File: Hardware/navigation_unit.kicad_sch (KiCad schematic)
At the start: 36 parts, among them SW1 SW_SPDT, SW2 SW_Push_Dual, U4 STM32F405RGTx, Y1 25MHz

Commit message: hardware version 0.1.2, minor improvements and footprint selection (missing some gnss and bulk regulator components
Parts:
- SW1: footprint (none) -> Button_Switch_SMD:SW_SPDT_PCM12
- SW2: footprint (none) -> Aircraft_Footprints:SW_SKRPACE010
- Y1: footprint (none) -> Crystal:Crystal_SMD_Abracon_ABM8G-4Pin_3.2x2.5mm
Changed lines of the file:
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@@
 	(title_block
 		(title "Navigation Unit")
-		(rev "0.1.0")
+		(rev "0.1.2")
 		(company "Breno Soares Alves")
 	)
@@
 			)
 		)
-		(property "Footprint" ""
+		(property "Footprint" "Button_Switch_SMD:SW_SPDT_PCM12"
 			(at 186.69 105.41 0)
 			(effects
@@
 			)
 		)
-		(property "Footprint" ""
+		(property "Footprint" "Aircraft_Footprints:SW_SKRPACE010"
 			(at 238.76 88.9 0)
 			(effects
@@
 			)
 		)
-		(property "Footprint" ""
+		(property "Footprint" "Crystal:Crystal_SMD_Abracon_ABM8G-4Pin_3.2x2.5mm"
 			(at 157.48 66.04 0)
 			(effects

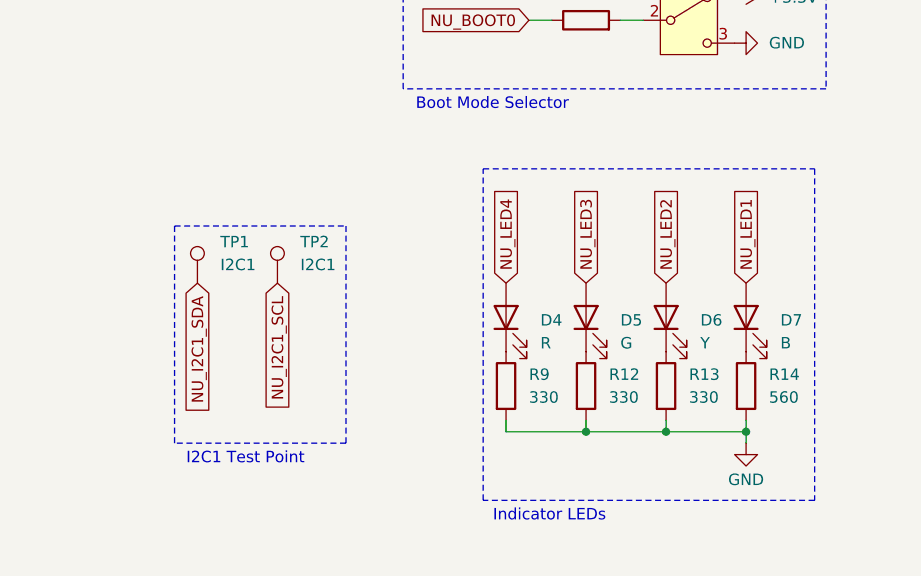
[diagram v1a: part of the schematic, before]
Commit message: board placement, no trails, just pain
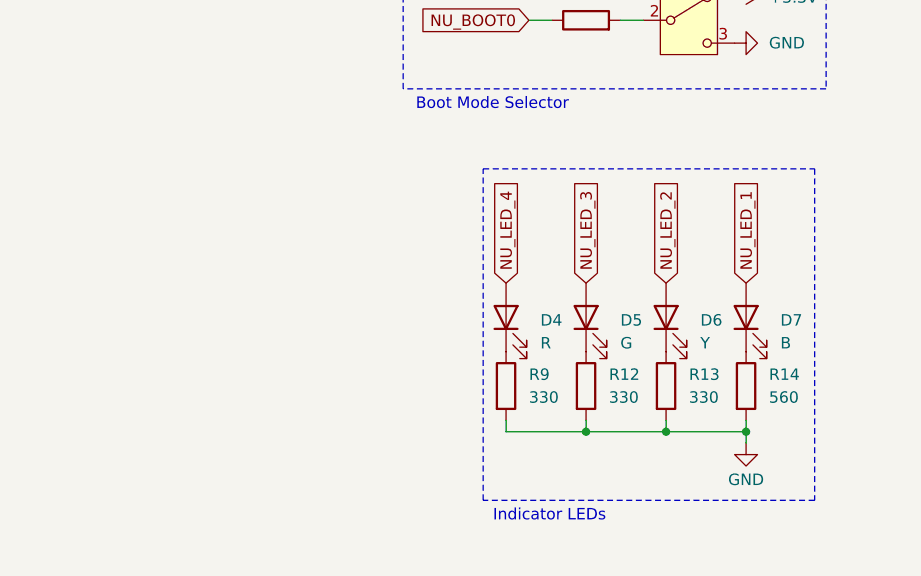
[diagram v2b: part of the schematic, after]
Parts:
- removed TP1, TP2: I2C1, TestPoint:TestPoint_Pad_D2.5mm, symbol Connector:TestPoint
- C12, C13: Digikey_Link (none) -> https://www.digikey.com.br/pt/products/detail/samsung-elect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; MPN (none) -> CL10B225KP8NNNC
- C14: footprint Capacitor_Tantalum_SMD:CP_EIA-1608-08_AVX-J -> Capacitor_SMD:C_1206_3216Metric_Pad1.33x1.80mm_HandSolder; Digikey_Link (none) -> https://www.digikey.com.br/pt/products/detail/kyocera-avx/T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; MPN (none) -> TAJA106K010TNJ
- C15, C18: Digikey_Link (none) -> https://www.digikey.com.br/pt/products/detail/w%C3%BCrth-el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; MPN (none) -> 885012005007
- C16, C17, C19, C20, C21, C22, C23, C24: Digikey_Link (none) -> https://www.digikey.com.br/pt/products/detail/samsung-elect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; MPN (none) -> CL05B104KP5NNNC
- C25: Digikey_Link (none) -> https://www.digikey.com.br/pt/products/detail/kemet/C0603C1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; MPN (none) -> C0603C104K8RACTU
- C26: Digikey_Link (none) -> https://www.digikey.com.br/pt/products/detail/kemet/T491A10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; MPN (none) -> T491A105K010AT
- D4: footprint LED_SMD:LED_0805_2012Metric -> LED_SMD:LED_0805_2012Metric_Pad1.15x1.40mm_HandSolder; Digikey_Link (none) -> https://www.digikey.com.br/pt/products/detail/liteon/LTST-C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; MPN (none) -> LTST-C171KRKT
- D5: footprint LED_SMD:LED_0805_2012Metric -> LED_SMD:LED_0805_2012Metric_Pad1.15x1.40mm_HandSolder; Digikey_Link (none) -> https://www.digikey.com.br/pt/products/detail/liteon/LTST-C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; MPN (none) -> LTST-C170GKT
- D6: footprint LED_SMD:LED_0805_2012Metric -> LED_SMD:LED_0805_2012Metric_Pad1.15x1.40mm_HandSolder; Digikey_Link (none) -> https://www.digikey.com.br/pt/products/detail/liteon/LTST-C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; MPN (none) -> LTST-C171YKT
- D7: footprint LED_SMD:LED_0805_2012Metric -> LED_SMD:LED_0805_2012Metric_Pad1.15x1.40mm_HandSolder; Digikey_Link (none) -> https://www.digikey.com.br/pt/products/detail/liteon/LTST-C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; MPN (none) -> LTST-C171TBKT
- FB1: footprint Inductor_SMD:L_0805_2012Metric -> Inductor_SMD:L_0805_2012Metric_Pad1.05x1.20mm_HandSolder; Digikey_Link (none) -> https://www.digikey.com.br/pt/products/detail/laird-signal-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; MPN (none) -> HZ0805E601R-10
- R10: Digikey_Link (none) -> https://www.digikey.com.br/pt/products/detail/yageo/RC0603F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; MPN (none) -> RC0603FR-07620RL
- R11: Digikey_Link (none) -> https://www.digikey.com.br/pt/products/detail/yageo/RC0603F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; MPN (none) -> RC0603FR-0710KL
- R12, R13, R9: Digikey_Link (none) -> https://www.digikey.com.br/pt/products/detail/yageo/RC0603J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; MPN (none) -> RC0603JR-07330RL
- R14: Digikey_Link (none) -> https://www.digikey.com.br/pt/products/detail/stackpole-ele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; MPN (none) -> RMCF0603FT560R
- R15, R16, R17, R18: Digikey_Link (none) -> https://www.digikey.com.br/pt/products/detail/panasonic-ele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; MPN (none) -> ERJ-3EKF4701V
- SW1: Digikey_Link (none) -> https://www.digikey.com.br/pt/products/detail/c-k/pcm12smtb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; MPN (none) -> PCM12SMTR
- SW2: footprint Aircraft_Footprints:SW_SKRPACE010 -> Aircraft_Footprints:SW4_PTS815 SJM 250 SMTR LFS_CNK; Digikey_Link (none) -> https://www.digikey.com.br/pt/products/detail/c-k/PTS815SJM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; MPN (none) -> PTS815SJM250SMTRLFS
- U4: Digikey_Link (none) -> https://www.digikey.com.br/pt/products/detail/stmicroelectr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; MPN (none) -> STM32F405RGT6
- Y1: Digikey_Link (none) -> https://www.digikey.com.br/pt/products/detail/abracon-llc/a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; MPN (none) -> ABM8G-25.000MHZ-B4Y-T3
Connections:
- net NU_LED1 is gone; now on net NU_LED_1: D7.2 (A)
- net NU_LED2 is gone; now on net NU_LED_2: D6.2 (A)
- net NU_LED3 is gone; now on net NU_LED_3: D5.2 (A)
- net NU_LED4 is gone; now on net NU_LED_4: D4.2 (A)
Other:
- note removed: "I2C1 Test Point"
